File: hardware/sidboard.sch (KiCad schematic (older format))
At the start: 33 parts, among them IC1 ATMEGA162-P, J1 AVR-ISP, J2 DB9, P1 AUDIO OUT, P2 DC 12V, P3 FAN, SW1 RESET, U1 6581 SID, U2 LM7805, U3 MAX232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

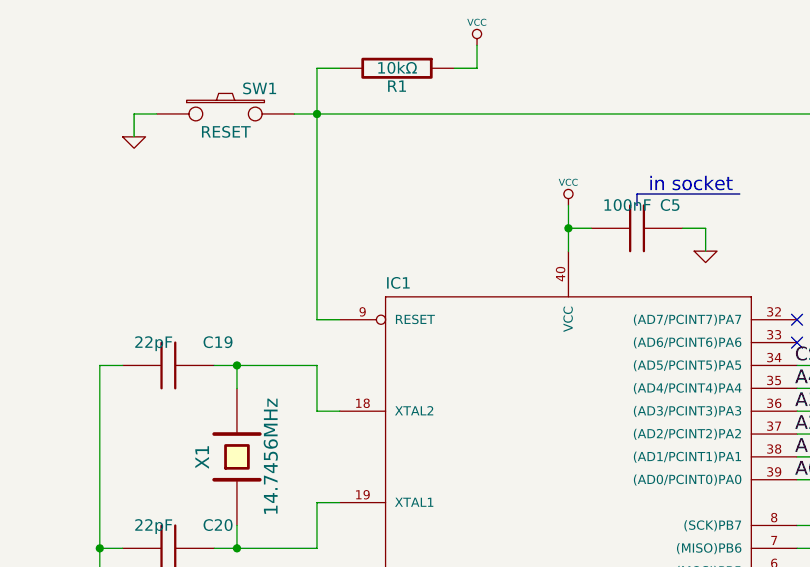
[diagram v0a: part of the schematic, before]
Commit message: fixed duplicate pins
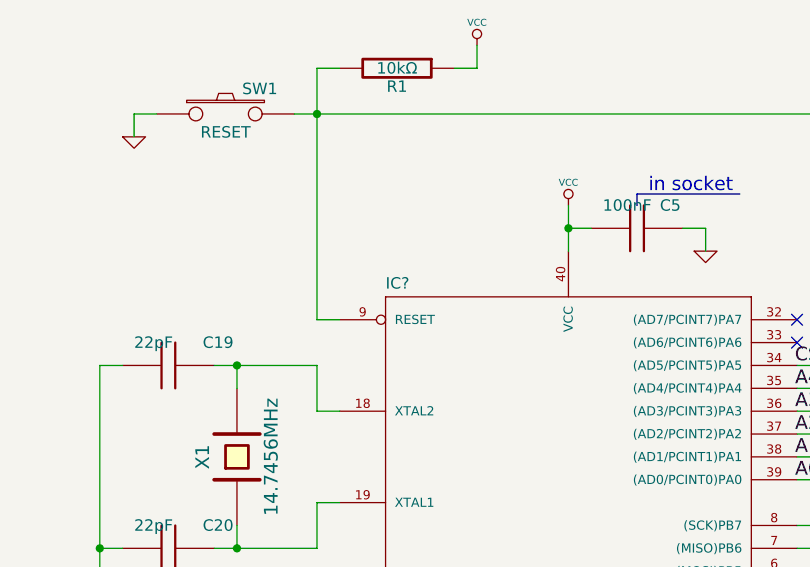
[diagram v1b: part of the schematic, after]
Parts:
- removed IC1: ATMEGA162-P, symbol ATMEGA162-P
- added IC?: ATMEGA162-P, DIL40, symbol ATMEGA162-P
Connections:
- net A0: now also IC?.39 ((AD0/PCINT0)PA0)
- net A1: now also IC?.38 ((AD1/PCINT1)PA1)
- net A2: now also IC?.37 ((AD2/PCINT2)PA2)
- net A3: now also IC?.36 ((AD3/PCINT3)PA3)
- net A4: now also IC?.35 ((AD4/PCINT4)PA4)
- net AVR_CTS: now also IC?.12 ((INT0/XCK1)PD2)
- net AVR_RTS: now also IC?.13 ((INT1/ICP3)PD3)
- net AVR_RX: now also IC?.10 ((RXD0)PD0)
- net AVR_TX: now also IC?.11 ((TXD0)PD1)
- net CS: now also IC?.34 ((AD5/PCINT5)PA5)
- net D0: now also IC?.21 ((A8/PCINT8)PC0)
- net D1: now also IC?.22 ((A9/PCINT9)PC1)
- net D2: now also IC?.23 ((A10/PCINT10)PC2)
- net D3: now also IC?.24 ((A11/PCINT11)PC3)
- net D4: now also IC?.25 ((A12/TCK/PCINT12)PC4)
- net D5: now also IC?.26 ((A13/TMS/PCINT13)PC5)
- net D6: now also IC?.27 ((A14/TDO/PCINT14)PC6)
- net D7: now also IC?.28 ((A15/TDI/PCINT15)PC7)
- net GND: now also IC?.20 (GND)
- net RES: now also IC?.31 ((ICP1/INT2)PE0)
- net RW: now also IC?.30 ((ALE)PE1)
- net VCC: now also IC?.40 (VCC)
- net at C19.1, X1.2: now also IC?.18 (XTAL2)
- net at C20.1, X1.1: now also IC?.19 (XTAL1)
- net at U1.6 (Ø2): now also IC?.2 ((OC2/T1)PB1), IC?.5 ((SS/OC3B)PB4)
- net at J1.1: now also IC?.6 ((MOSI)PB5)
- net at J1.9: now also IC?.7 ((MISO)PB6)
- net at J1.7: now also IC?.8 ((SCK)PB7)
- net at J1.5, R1.2, SW1.2: now also IC?.9 (RESET)
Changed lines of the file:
@@
-EESchema Schematic File Version 2  date Sun 22 Apr 2012 01:56:48 PM CEST
+EESchema Schematic File Version 2  date Sun 22 Apr 2012 02:24:51 PM CEST
 LIBS:power
 LIBS:device
@@
 LIBS:atmega162
 LIBS:6581_sid
-EELAYER 43  0
+EELAYER 24  0
 EELAYER END
 $Descr A4 11700 8267
@@
 Comment4 ""
 $EndDescr
+$Comp
+L ATMEGA162-P IC?
+U 1 1 4F93F890
+P 4450 3800
+F 0 "IC?" H 3650 5530 50  0000 L BNN
+F 1 "ATMEGA162-P" H 4675 1400 50  0000 L BNN
+F 2 "DIL40" H 4950 1325 50  0001 C CNN
+	1    4450 3800
+	1    0    0    -1
+$EndComp
 Text Label 5500 5900 0    60   ~ 0
 RW
@@
 	1    0    0    -1
 $EndComp
-$Comp
-L ATMEGA162-P IC1
-U 1 1 4F93CC65
-P 4450 3800
-F 0 "IC1" H 3650 5530 50  0000 L BNN
-F 1 "ATMEGA162-P" H 4675 1400 50  0000 L BNN
-	1    4450 3800
-	1    0    0    -1
-$EndComp
